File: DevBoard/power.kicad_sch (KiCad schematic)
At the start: 29 parts, among them J201 SMA OUT_LO, J202 SMA OUT_HI, U201 INA190A5IDDFR, U202 INA190A1IDDFR, U203 TPS70950DBVR, U204 TPS62177DQCR

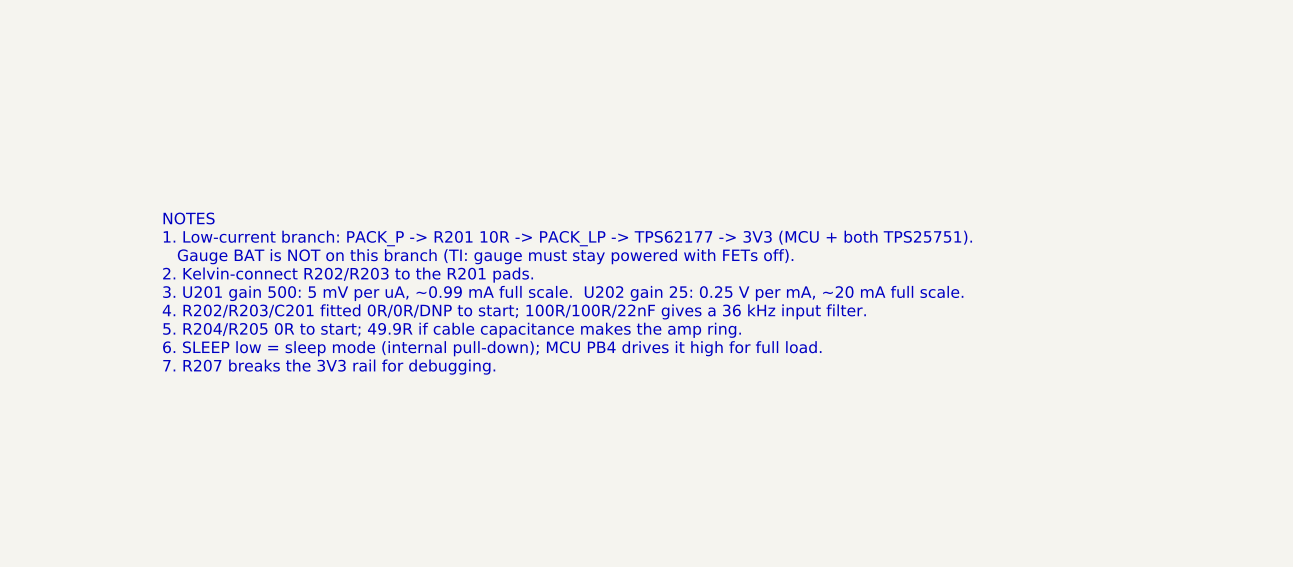
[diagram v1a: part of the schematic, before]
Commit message: Dev board: hand-solder the INA190s, keep PPHV bulk with soft-start
- U201/U202 sourced from DigiKey/Mouser and hand-soldered: excluded from the
  position file, LCSC removed, MPN and Sourcing properties added, sheet note
- PPHV bulk above 100 uF justified by the TPS25751D sink soft-start (inrush
  ~0.1 A at setting 0); sheet note asks for SS setting 0 or 1 in config
- README and circuit description updated

Co-Authored-By: Claude Opus 5.5 <noreply@anthropic.com>
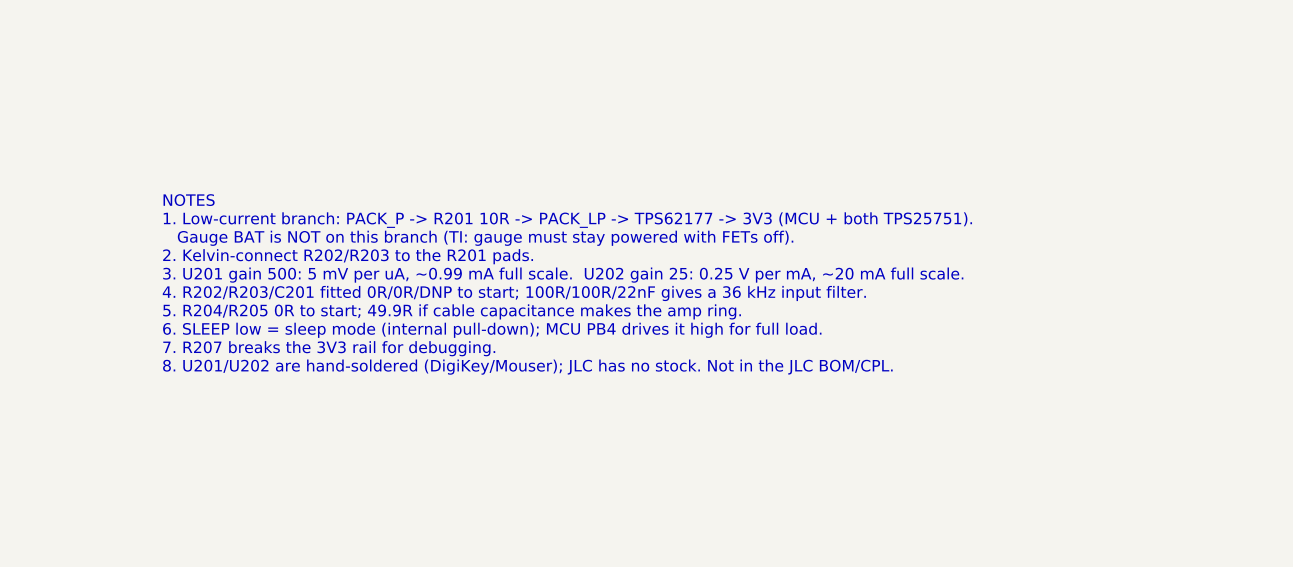
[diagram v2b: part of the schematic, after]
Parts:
- U201: MPN (none) -> TI INA190A5IDDFR; Sourcing (none) -> DigiKey/Mouser, hand-solder (not JLC assembled)
- U202: LCSC C1852068 -> (none); MPN (none) -> TI INA190A1IDDFR; Sourcing (none) -> DigiKey/Mouser, hand-solder (not JLC assembled)
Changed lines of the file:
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@@
 		)
 	)
-	(text "NOTES\n1. Low-current branch: PACK_P -> R201 10R -> PACK_LP -> TPS62177 -> 3V3 (MCU + both TPS25751).\n   Gauge BAT is NOT on this branch (TI: gauge must stay powered with FETs off).\n2. Kelvin-connect R202/R203 to the R201 pads.\n3. U201 gain 500: 5 mV per uA, ~0.99 mA full scale.  U202 gain 25: 0.25 V per mA, ~20 mA full scale.\n4. R202/R203/C201 fitted 0R/0R/DNP to start; 100R/100R/22nF gives a 36 kHz input filter.\n5. R204/R205 0R to start; 49.9R if cable capacitance makes the amp ring.\n6. SLEEP low = sleep mode (internal pull-down); MCU PB4 drives it high for full load.\n7. R207 breaks the 3V3 rail for debugging."
+	(text "NOTES\n1. Low-current branch: PACK_P -> R201 10R -> PACK_LP -> TPS62177 -> 3V3 (MCU + both TPS25751).\n   Gauge BAT is NOT on this branch (TI: gauge must stay powered with FETs off).\n2. Kelvin-connect R202/R203 to the R201 pads.\n3. U201 gain 500: 5 mV per uA, ~0.99 mA full scale.  U202 gain 25: 0.25 V per mA, ~20 mA full scale.\n4. R202/R203/C201 fitted 0R/0R/DNP to start; 100R/100R/22nF gives a 36 kHz input filter.\n5. R204/R205 0R to start; 49.9R if cable capacitance makes the amp ring.\n6. SLEEP low = sleep mode (internal pull-down); MCU PB4 drives it high for full load.\n7. R207 breaks the 3V3 rail for debugging.\n8. U201/U202 are hand-soldered (DigiKey/Mouser); JLC has no stock. Not in the JLC BOM/CPL."
 		(exclude_from_sim no)
 		(at 215.9 129.54 0)
@@
 		(dnp no)
 		(property "Reference" "TP203"
-			(at 190.50 159.25 0)
+			(at 190.5 159.25 0)
 			(show_name no)
 			(do_not_autoplace no)
@@
 		)
 		(property "Value" "GND"
-			(at 190.50 169.42 0)
+			(at 190.5 169.42 0)
 			(show_name no)
 			(do_not_autoplace no)
@@
 		)
 		(property "Value" "0R"
-			(at 65.89 136.90 90)
+			(at 65.89 136.9 90)
 			(show_name no)
 			(do_not_autoplace no)
@@
 		(in_bom yes)
 		(on_board yes)
-		(in_pos_files yes)
+		(in_pos_files no)
 		(dnp no)
 		(property "Reference" "U201"
@@
 			)
 		)
+		(property "MPN" "TI INA190A5IDDFR"
+			(at 109.22 144.78 0)
+			(hide yes)
+			(show_name no)
+			(do_not_autoplace no)
+			(effects
+				(font
+					(size 1.27 1.27)
+				)
+			)
+		)
+		(property "Sourcing" "DigiKey/Mouser, hand-solder (not JLC assembled)"
+			(at 109.22 144.78 0)
+			(hide yes)
+			(show_name no)
+			(do_not_autoplace no)
+			(effects
+				(font
+					(size 1.27 1.27)
+				)
+			)
+		)
 		(pin "1"
 		)
@@
 		)
 		(property "Value" "GND"
-			(at 152.40 83.06 0)
+			(at 152.4 83.06 0)
 			(show_name no)
 			(do_not_autoplace no)
@@
 		(dnp no)
 		(property "Reference" "TP201"
-			(at 152.40 138.93 0)
+			(at 152.4 138.93 0)
 			(show_name no)
 			(do_not_autoplace no)
@@
 		)
 		(property "Value" "GND"
-			(at 165.10 67.82 0)
+			(at 165.1 67.82 0)
 			(show_name no)
 			(do_not_autoplace no)
@@
 		)
 		(property "Value" "GND"
-			(at 88.90 241.81 0)
+			(at 88.9 241.81 0)
 			(show_name no)
 			(do_not_autoplace no)
@@
 		(dnp no)
 		(property "Reference" "JP202"
-			(at 50.80 223.07 0)
+			(at 50.8 223.07 0)
 			(show_name no)
 			(do_not_autoplace no)
@@
 		)
 		(property "Value" "Meas. section power"
-			(at 50.80 225.04 0)
+			(at 50.8 225.04 0)
 			(show_name no)
 			(do_not_autoplace no)
@@
 		)
 		(property "Value" "GND"
-			(at 190.50 71.63 0)
+			(at 190.5 71.63 0)
 			(show_name no)
 			(do_not_autoplace no)
@@
 		(dnp no)
 		(property "Reference" "U203"
-			(at 88.90 223.58 0)
+			(at 88.9 223.58 0)
 			(show_name no)
 			(do_not_autoplace no)
@@
 		)
 		(property "Value" "TPS70950DBVR"
-			(at 88.90 225.55 0)
+			(at 88.9 225.55 0)
 			(show_name no)
 			(do_not_autoplace no)
@@
 		(dnp no)
 		(property "Reference" "U204"
-			(at 152.40 49.59 0)
+			(at 152.4 49.59 0)
 			(show_name no)
 			(do_not_autoplace no)
@@
 		)
 		(property "Value" "TPS62177DQCR"
-			(at 152.40 51.56 0)
+			(at 152.4 51.56 0)
 			(show_name no)
 			(do_not_autoplace no)
@@
 		(in_bom yes)
 		(on_board yes)
-		(in_pos_files yes)
+		(in_pos_files no)
 		(dnp no)
 		(property "Reference" "U202"
@@
 			)
 		)
-		(property "LCSC" "C1852068"
+		(property "MPN" "TI INA190A1IDDFR"
+			(at 109.22 182.88 0)
+			(hide yes)
+			(show_name no)
+			(do_not_autoplace no)
+			(effects
+				(font
+					(size 1.27 1.27)
+				)
+			)
+		)
+		(property "Sourcing" "DigiKey/Mouser, hand-solder (not JLC assembled)"
 			(at 109.22 182.88 0)
 			(hide yes)
@@
 		(dnp no)
 		(property "Reference" "TP202"
-			(at 152.40 177.03 0)
+			(at 152.4 177.03 0)
 			(show_name no)
 			(do_not_autoplace no)

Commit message: Dev board rev A4: design-review fixes, polymer bulk, charge inhibit
Schematic design review (three reviewers, cross-challenged) in
docs/devboard/schematic-review-2026-10-12.md, and its fixes:
- U203 TPS70950 EN no longer tied to PACK_P (would destroy it)
- ICHG 17.8k: 2.8 A per port (was 9.8 A, above the cells' 5.6 A)
- U101 footprint from TI RSM0032A (1.4 mm thermal pad, was 2.8 mm)
- D+/D- ESD now 5 V PESD5V0S2BT (TPS25751 GPIO4/5 are rated 6 V)
- R101-R104 1206, F101 and J101 DNP, DNP gate parts on Q102
- BTP_INT buffered by a 2N7002; SMBus pull-ups on a removable 0R
- Wake button, bench PACK_P header, reset, BOOT0/3V3_SLEEP pads,
  J303 series resistors, IRQ pull-ups, vertical SMAs, BOM ratings

Open-question decisions: CHG_INH (PB8 -> each BQ25756 CE) lets the
MCU stop charging independently of the TPS25751; J103 in EV2400
SMBus pin order; "fit cells before USB" silkscreen.

Charger bulk banks now one solid polymer cap plus the MLCCs at the
FETs (16 fewer MLCCs). PWR_FLAGs moved to where each rail is sourced.
Board: footprints swapped/added and placed, DRC clean before routing.

Co-Authored-By: Claude Opus 5.5 <noreply@anthropic.com>
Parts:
- C202, C203: value 0.1u -> 0.1u 50V; LCSC (none) -> C14663; MPN (none) -> CC0603KRX7R9BB104
- C205: value 2.2u 10V -> 4.7u 25V; footprint Capacitor_SMD:C_0603_1608Metric -> Capacitor_SMD:C_0805_2012Metric; LCSC (none) -> C1779; MPN (none) -> CL21A475KAQNNNE; Notes (none) -> TPS709 needs >= 1.5 uF effective at 5 V (review m3)
- J201, J202: footprint Connector_Coaxial:SMA_Amphenol_132289_EdgeMount -> Connector_Coaxial:SMA_Amphenol_132134_Vertical; MPN (none) -> Amphenol 132134 (or any 5-pin vertical SMA-KE); Notes (none) -> Vertical SMA: the edge-launch 132289 needs a 1.6 mm board (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
- JP202: LCSC (none) -> C492401; MPN (none) -> PZ254V-11-02P
- R201: value 10R 1% 0.5W -> 10R 1%; LCSC (none) -> C17903; MPN (none) -> 1206W4F100JT5E; Notes R_MEAS -> R_MEAS: <= 10 mA in use (1 mW); 0.4 W for ~0.35 ms at TPS62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
- R204, R205: value 0R -> 49.9; LCSC (none) -> C23185; MPN (none) -> 0603WAF499JT5E; Notes 49.9R option -> Isolates the INA190 output from cable capacitance (max 1 nF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
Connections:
- net GND: now also U204.4 (NC)
- net LDO_IN: no longer U203.3 (EN)

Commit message: Dev board rev A5: BAT fed before F101, review 2 hardware fixes, JLC passives
- Gauge BAT feed follows TI fig. 9-12: D101 from the cell top (CELL_P_RAW)
  before F101, so the gauge stays powered if the fuse opens or is unfitted.
- C421/C521 100 uF 35 V polymer (same 6.3 mm footprint): about 99 uF worst
  case vs the BQ25756 80 uF minimum after derating.
- Bootstrap diodes LRB520S-40T1G, Q103 BSS138, DNP C109 4.7 nF (fit D103
  with it), PPHV 0.1 uF and VBUS 10 nF per port, R306 330R, C201 DNP flag.
- Test points: GND loops by each port's SW probes and in the pack probe
  field, CELL_P_RAW, CE_N, LDO_3V3, LDO_IN, 5V_AMP.
- JLC part numbers on every resistor and capacitor.
- Placement for the new parts; placer hides test-point labels with no
  free spot. DRC clean, schematic parity clean.

Co-Authored-By: Claude Opus 5.5 <noreply@anthropic.com>
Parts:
- added TP206: LDO_IN, TestPoint:TestPoint_Pad_D1.5mm, symbol Connector:TestPoint
- added TP207: 5V_AMP, TestPoint:TestPoint_Pad_D1.5mm, symbol Connector:TestPoint
- C201: value 22n DNP -> 22n 50V; LCSC (none) -> C21122; MPN (none) -> CL10B223KB8NNNC; Notes (none) -> DNP (was marked DNP in its value only): optional INA190 inp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; now not fitted
- C204: LCSC (none) -> C28323; MPN (none) -> CL21B105KBFNNNE
- C206: LCSC (none) -> C2762602; MPN (none) -> CL21B225KBYNNNE
- C207: value 22u 10V -> 22u 25V; LCSC (none) -> C45783; MPN (none) -> CL21A226MAQNNNE
- R202, R203: LCSC (none) -> C21189; MPN (none) -> 0603WAF0000T5E
- R206, R208: LCSC (none) -> C25803; MPN (none) -> 0603WAF1003T5E
- R207: LCSC (none) -> C17477; MPN (none) -> 0805W8F0000T5E
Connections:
- net 5V_AMP: now also TP207.1
- net LDO_IN: now also TP206.1

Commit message: Dev board: SMD test loops (RH-S2761-46R) instead of Keystone through-hole
All 45 loop test points become ronghe RH-S2761-46R (LCSC C55121754), the
JLC-stocked equivalent of the Harwin S2761-46R: 1.6 x 0.8 x 1.15 mm SMT
loop on an 0603 land pattern, 3.5 A. New footprint
MonolithDev:TestPoint_Harwin_S2761_0603 (make_footprints.py section 11),
both pads pin 1 and jumpered. JLC places them; no through-hole assembly.

Co-Authored-By: Claude Opus 5.5 <noreply@anthropic.com>
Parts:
- TP201, TP202, TP203, TP204, TP205: footprint TestPoint:TestPoint_Keystone_5000-5004_Miniature -> MonolithDev:TestPoint_Harwin_S2761_0603; LCSC (none) -> C55121754; MPN (none) -> RH-S2761-46R (ronghe; Harwin S2761-46R equivalent)
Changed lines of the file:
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@@
 			)
 		)
-		(property "Footprint" "TestPoint:TestPoint_Keystone_5000-5004_Miniature"
+		(property "Footprint" "MonolithDev:TestPoint_Harwin_S2761_0603"
 			(at 195.58 165.1 0)
 			(hide yes)
@@
 			)
 		)
+		(property "LCSC" "C55121754"
+			(at 190.5 165.1 0)
+			(hide yes)
+			(show_name no)
+			(do_not_autoplace no)
+			(effects
+				(font
+					(size 1.27 1.27)
+				)
+			)
+		)
+		(property "MPN" "RH-S2761-46R (ronghe; Harwin S2761-46R equivalent)"
+			(at 190.5 165.1 0)
+			(hide yes)
+			(show_name no)
+			(do_not_autoplace no)
+			(effects
+				(font
+					(size 1.27 1.27)
+				)
+			)
+		)
 		(pin "1"
 		)
@@
 			)
 		)
-		(property "Footprint" "TestPoint:TestPoint_Keystone_5000-5004_Miniature"
+		(property "Footprint" "MonolithDev:TestPoint_Harwin_S2761_0603"
 			(at 132.08 68.58 0)
 			(hide yes)
@@
 			)
 		)
+		(property "LCSC" "C55121754"
+			(at 127 68.58 0)
+			(hide yes)
+			(show_name no)
+			(do_not_autoplace no)
+			(effects
+				(font
+					(size 1.27 1.27)
+				)
+			)
+		)
+		(property "MPN" "RH-S2761-46R (ronghe; Harwin S2761-46R equivalent)"
+			(at 127 68.58 0)
+			(hide yes)
+			(show_name no)
+			(do_not_autoplace no)
+			(effects
+				(font
+					(size 1.27 1.27)
+				)
+			)
+		)
 		(pin "1"
 		)
@@
 			)
 		)
-		(property "Footprint" "TestPoint:TestPoint_Keystone_5000-5004_Miniature"
+		(property "Footprint" "MonolithDev:TestPoint_Harwin_S2761_0603"
 			(at 111.76 55.88 0)
 			(hide yes)
@@
 			)
 		)
+		(property "LCSC" "C55121754"
+			(at 106.68 55.88 0)
+			(hide yes)
+			(show_name no)
+			(do_not_autoplace no)
+			(effects
+				(font
+					(size 1.27 1.27)
+				)
+			)
+		)
+		(property "MPN" "RH-S2761-46R (ronghe; Harwin S2761-46R equivalent)"
+			(at 106.68 55.88 0)
+			(hide yes)
+			(show_name no)
+			(do_not_autoplace no)
+			(effects
+				(font
+					(size 1.27 1.27)
+				)
+			)
+		)
 		(pin "1"
 		)
@@
 			)
 		)
-		(property "Footprint" "TestPoint:TestPoint_Keystone_5000-5004_Miniature"
+		(property "Footprint" "MonolithDev:TestPoint_Harwin_S2761_0603"
 			(at 157.48 144.78 0)
 			(hide yes)
@@
 			)
 		)
+		(property "LCSC" "C55121754"
+			(at 152.4 144.78 0)
+			(hide yes)
+			(show_name no)
+			(do_not_autoplace no)
+			(effects
+				(font
+					(size 1.27 1.27)
+				)
+			)
+		)
+		(property "MPN" "RH-S2761-46R (ronghe; Harwin S2761-46R equivalent)"
+			(at 152.4 144.78 0)
+			(hide yes)
+			(show_name no)
+			(do_not_autoplace no)
+			(effects
+				(font
+					(size 1.27 1.27)
+				)
+			)
+		)
 		(pin "1"
 		)
@@
 			)
 		)
-		(property "Footprint" "TestPoint:TestPoint_Keystone_5000-5004_Miniature"
+		(property "Footprint" "MonolithDev:TestPoint_Harwin_S2761_0603"
 			(at 157.48 182.88 0)
 			(hide yes)
@@
 			(at 152.4 182.88 0)
 			(hide yes)
+			(show_name no)
+			(do_not_autoplace no)
+			(effects
+				(font
+					(size 1.27 1.27)
+				)
+			)
+		)
+		(property "LCSC" "C55121754"
+			(at 152.4 182.88 0)
+			(hide yes)
+			(show_name no)
+			(do_not_autoplace no)
+			(effects
+				(font
+					(size 1.27 1.27)
+				)
+			)
+		)
+		(property "MPN" "RH-S2761-46R (ronghe; Harwin S2761-46R equivalent)"
+			(at 152.4 182.88 0)
+			(hide yes)

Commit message: Dev board: open-item pass, J104 diode, antenna keep-out, bring-up checklist
- D104 SS34 in series with the J104 bench input (reversed lead, back-feed).
- ANT_KEEPOUT rule area (no tracks/vias/pours, all copper layers) around
  the STM32WB1MMC antenna end, created by place_parts.py.
- D401 drawn unidirectional; header part numbers (PZ254V-11 family);
  shunt, J301 keying, B-constant, insulated-NTC, sheet-text and R201 notes.
- docs/devboard/bringup-config-checklist.md: every configuration item from
  both reviews in bring-up order, with review 2's precharge correction;
  review 1's 0 mV precharge line marked superseded.

Co-Authored-By: Claude Opus 5.5 <noreply@anthropic.com>
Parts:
- JP201: LCSC (none) -> C492401; MPN (none) -> PZ254V-11-02P; Notes pull = amps off -> pull = amps off. Needs a 2.54 mm shunt (hand, not in the JL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
- JP202: Notes (none) -> Fit a 2.54 mm shunt (hand, not in the JLC BOM) to power the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
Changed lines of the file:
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@@
+			)
+		)
+		(property "Notes" "Fit a 2.54 mm shunt (hand, not in the JLC BOM) to power the measurement section"
+			(at 50.8 229.87 0)
+			(hide yes)
+			(show_name no)
+			(do_not_autoplace no)
+			(effects
+				(font
+					(size 1.27 1.27)
+				)
 			)
 		)
@@
 			)
 		)
-		(property "Notes" "pull = amps off"
+		(property "Notes" "pull = amps off. Needs a 2.54 mm shunt (hand, not in the JLC BOM)"
 			(at 0 0 0)
 			(hide yes)
 			(show_name no)
+			(do_not_autoplace no)
+			(effects
+				(font
+					(size 1.27 1.27)
+				)
+			)
+		)
+		(property "LCSC" "C492401"
+			(at 132.08 229.87 0)
+			(hide yes)
+			(show_name no)
+			(do_not_autoplace no)
+			(effects
+				(font
+					(size 1.27 1.27)
+				)
+			)
+		)
+		(property "MPN" "PZ254V-11-02P"
+			(at 132.08 229.87 0)
+			(hide yes)
+			(show_name no)
